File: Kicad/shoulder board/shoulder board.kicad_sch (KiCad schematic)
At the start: 3 parts, among them J1 Conn_01x03, SW1 TC-1102N-C-DL-B, SW2 TC-1102N-C-DL-B

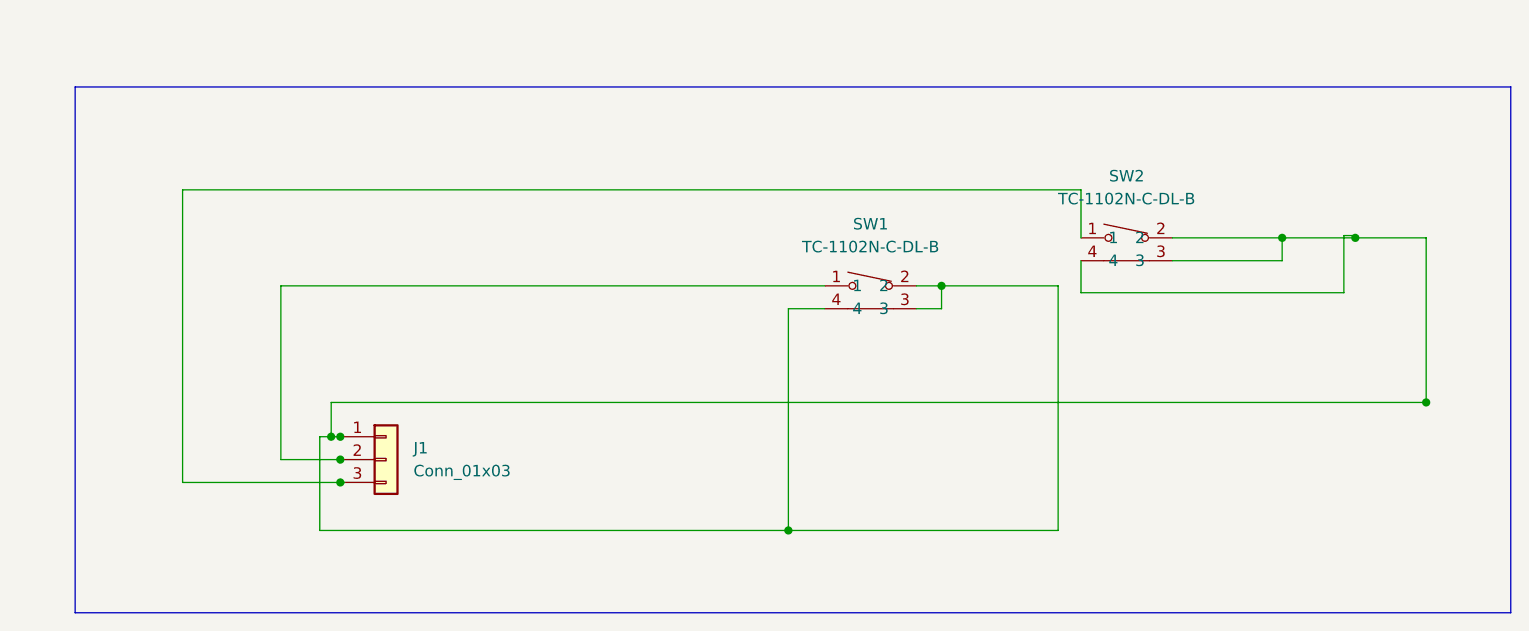
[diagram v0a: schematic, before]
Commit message: changes in schematic to add vibration motors for controller and led
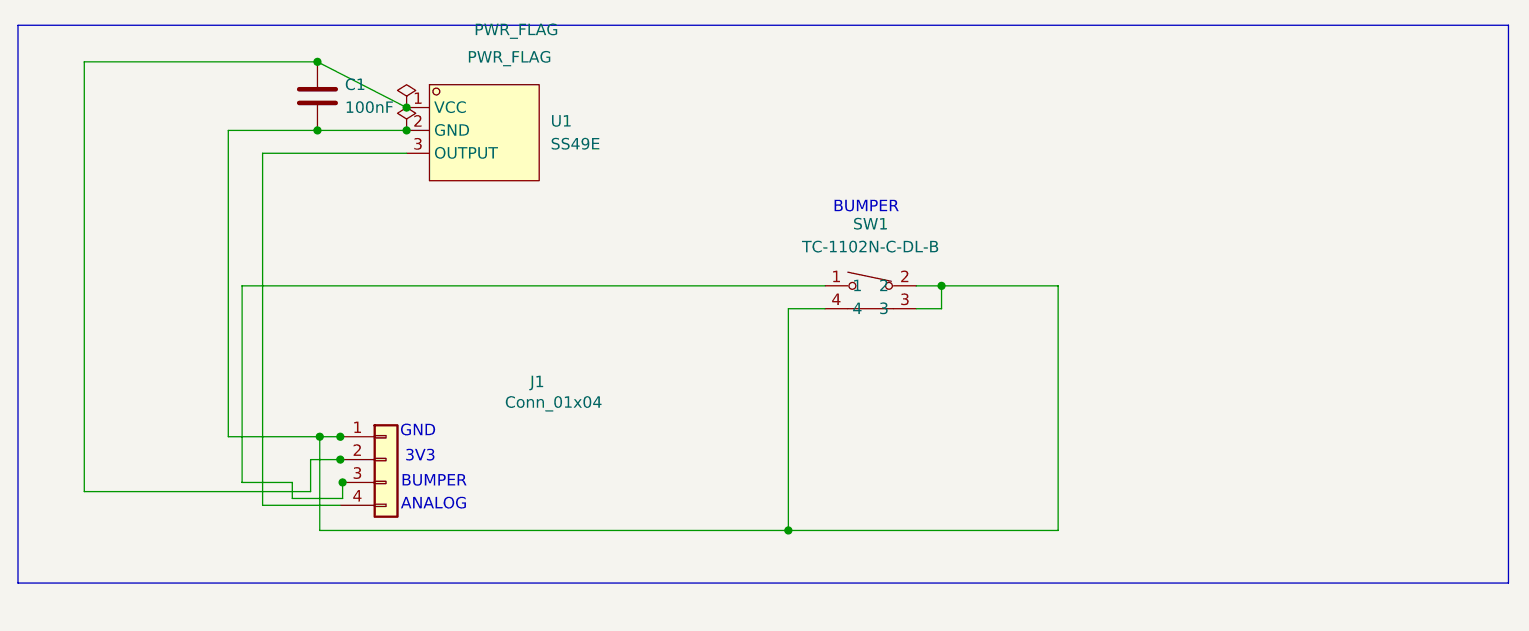
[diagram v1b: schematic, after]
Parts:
- removed J1: Conn_01x03, Connector_JST:JST_XH_B3B-XH-A_1x03_P2.50mm_Vertical, symbol Connector_Generic:Conn_01x03
- removed SW2: TC-1102N-C-DL-B, easyeda2kicad:SW-TH_TC-1102N-C-DL-B, symbol easyeda2kicad:TC-1102N-C-DL-B
- added C1: 100nF, symbol Device:C
- added J1: Conn_01x04, Connector_JST:JST_XH_B4B-XH-A_1x04_P2.50mm_Vertical, symbol Connector_Generic:Conn_01x04
- added U1: SS49E, easyeda2kicad:TO-92S_3P-L4.1-W1.6-P1.27-L, symbol easyeda2kicad:SS49E
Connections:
- net at SW1.1: now also J1.3 (Pin_3)
- net at SW1.2, SW1.3, SW1.4: now also C1.1, J1.1 (Pin_1), U1.2 (GND)
- new net: C1.2, J1.2 (Pin_2), U1.1 (VCC)
- new net: J1.4 (Pin_4), U1.3 (OUTPUT)
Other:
- note added: "3V3"
- note added: "ANALOG"
- note added: "BUMPER"
- note added: "GND"
